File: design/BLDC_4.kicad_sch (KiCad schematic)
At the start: 26 parts, among them K1 SERVO, P1 HALL/Encoder, P101 CANBUS, P3 PWR_COMM, P4 IN+, P5 IN-, P6 MOTOR1, P7 MOTOR2, P9 MOTOR3, X1 MINI-USB-SHIELD-32005-201

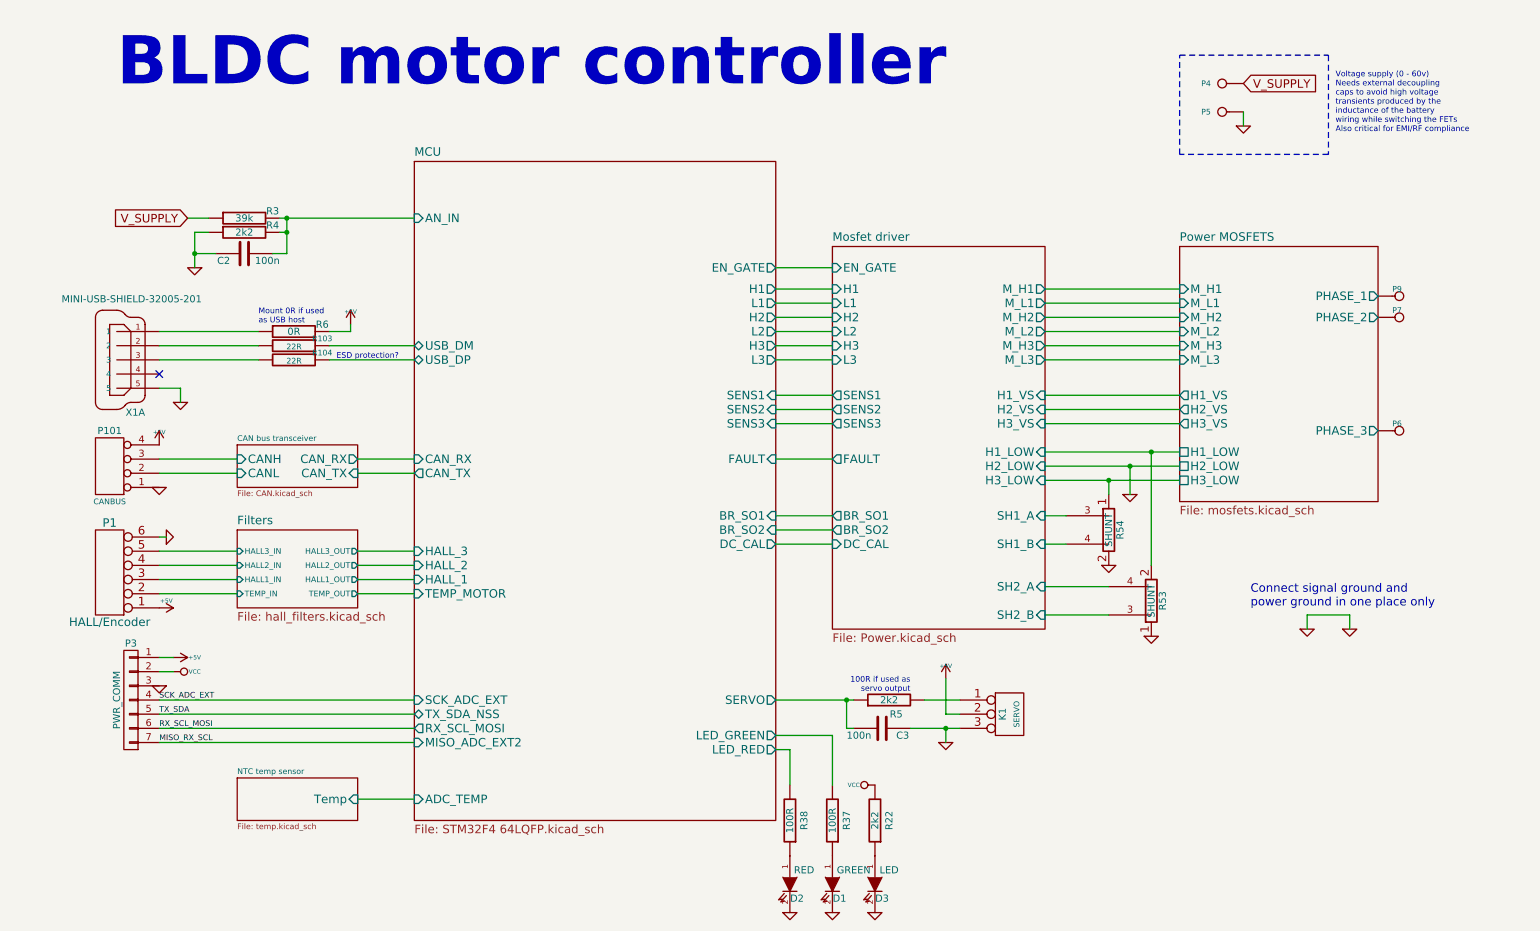
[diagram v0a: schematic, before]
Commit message: Eliminado módulo CAN, agregado módulo bluetooth
Eliminado de hoja CAN, añadido de módulo bluetooth
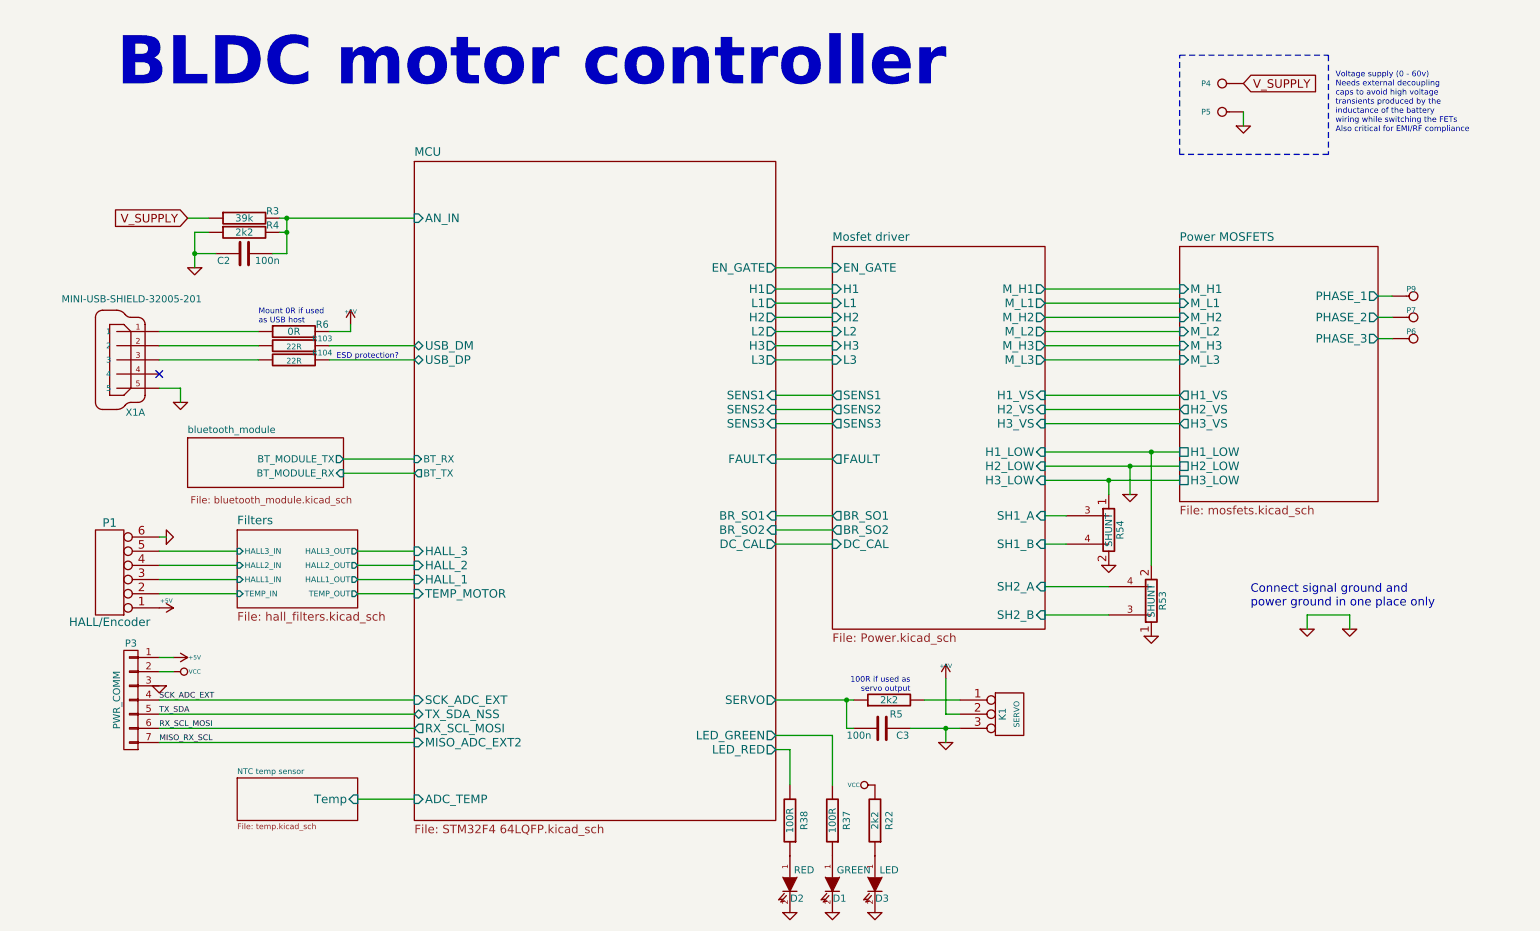
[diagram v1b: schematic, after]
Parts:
- removed P101: CANBUS, JST conn:b4b-ph-kl, symbol BLDC_4-rescue1:CONN_4
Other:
- removed sheet CAN bus transceiver
- added sheet bluetooth_module (bluetooth_module.kicad_sch)
- sheet MCU ports: added BT_RX, BT_TX; removed CAN_RX, CAN_TX
- moved on the sheet: P6, P7, P9
